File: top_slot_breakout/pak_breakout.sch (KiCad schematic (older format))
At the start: 19 parts, among them J1 Conn_02x08_Odd_Even, J2 Conn_01x06_Female, J3 Conn_01x04_Female, J4 Conn_01x02_Female, J5 Conn_01x03_Female, J6 Conn_01x12_Female, U1 74LS245, U2 74LS245, U3 Pico

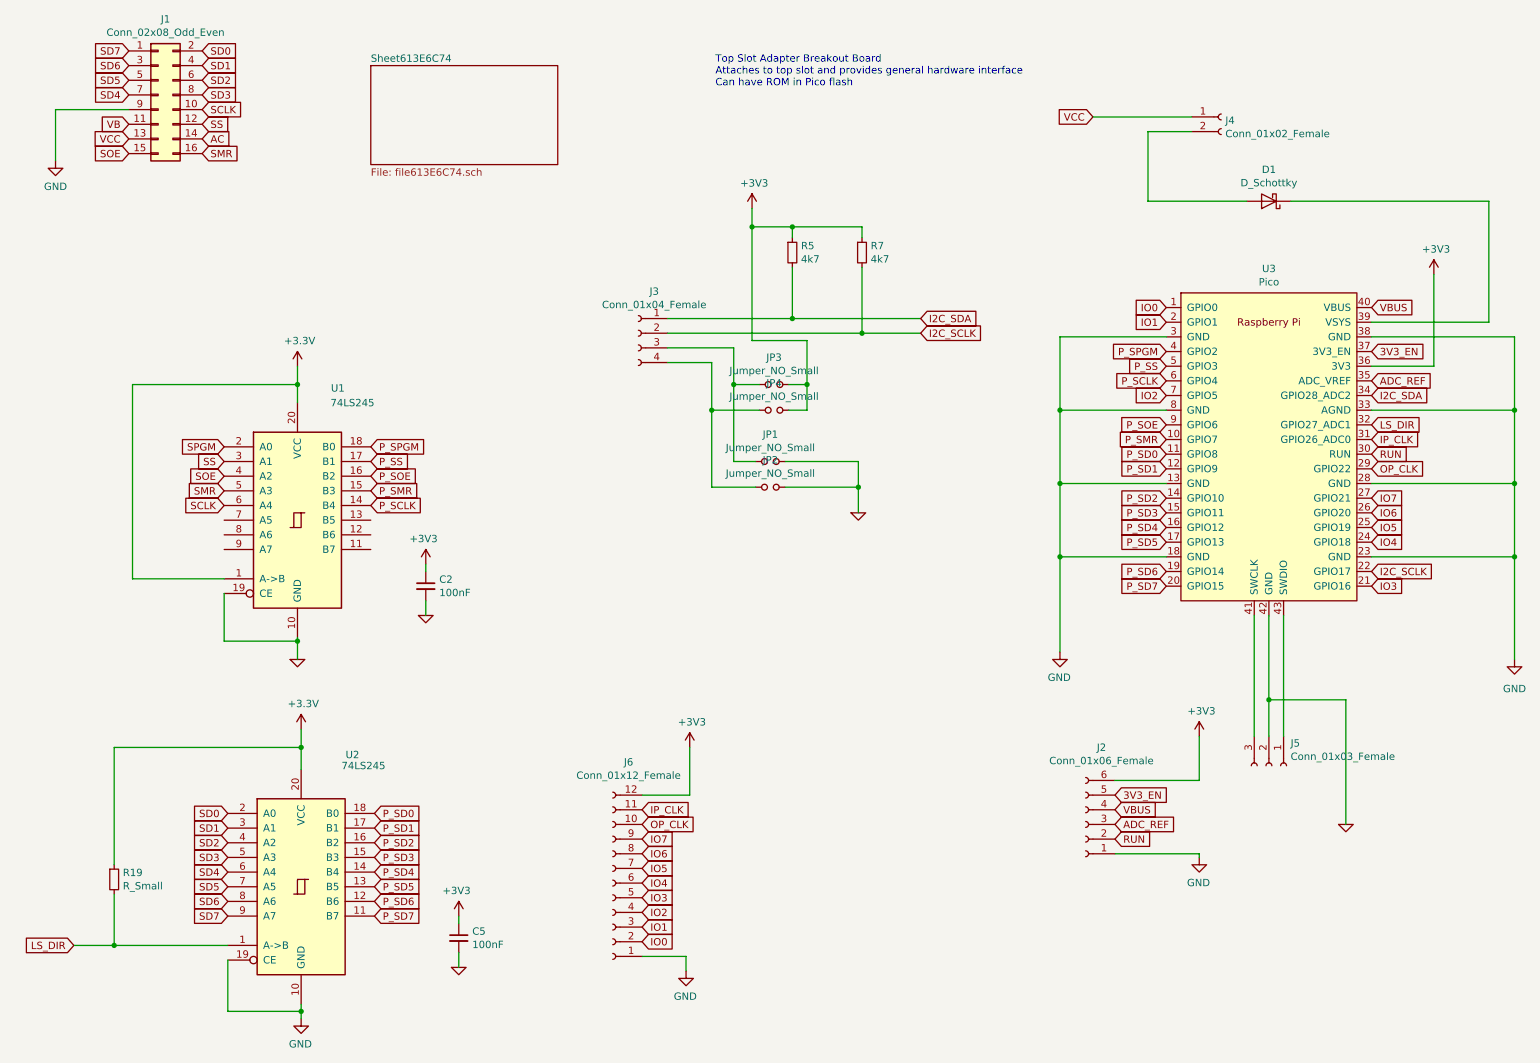
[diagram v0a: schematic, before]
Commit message: Added code based on (identical to) pak-gadget
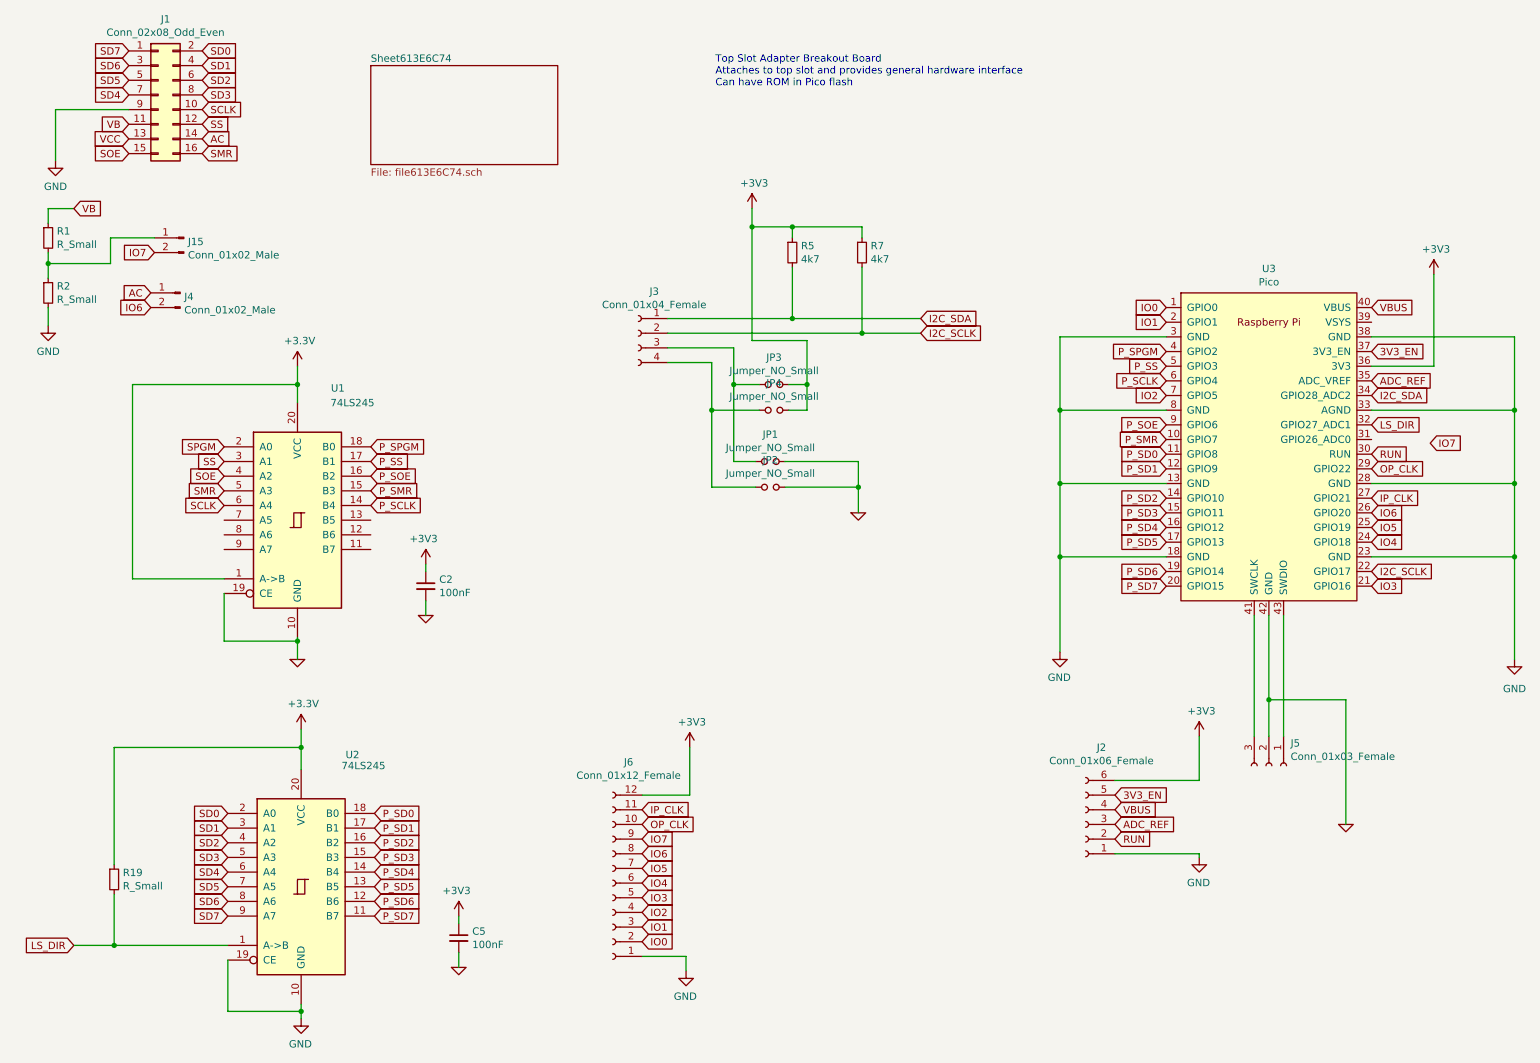
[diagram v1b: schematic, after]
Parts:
- removed D1: D_Schottky, Diode_SMD:D_SOD-123, symbol Device:D_Schottky
- removed J4: Conn_01x02_Female, Connector_PinHeader_2.54mm:PinHeader_1x02_P2.54mm_Vertical, symbol Connector:Conn_01x02_Female
- added J15, J4: Conn_01x02_Male, Connector_PinHeader_2.54mm:PinHeader_1x02_P2.54mm_Vertical, symbol Connector:Conn_01x02_Male
- added R1, R2: R_Small, Resistor_SMD:R_0805_2012Metric, symbol Device:R_Small
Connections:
- net AC: now also J4.1 (Pin_1)
- net GND: now also R2.2
- net IO6: now also J4.2 (Pin_2)
- net IO7: now also J15.2 (Pin_2); no longer U3.27 (GPIO21)
- net IP_CLK: now also U3.27 (GPIO21); no longer U3.31 (GPIO26_ADC0)
- net VB: now also R1.1
- new net: J15.1 (Pin_1), R1.2, R2.1
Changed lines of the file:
@@
 Wire Wire Line
 	3525 6975 3525 7075
-Wire Wire Line
-	9200 1850 10550 1850
-Wire Wire Line
-	10550 1850 10550 2675
-Wire Wire Line
-	10550 2675 9750 2675
-Wire Wire Line
-	8900 1850 8225 1850
-Wire Wire Line
-	8225 1850 8225 1375
-Wire Wire Line
-	8225 1375 8525 1375
-Text GLabel 7850 1275 0    50   Input ~ 0
-VCC
-Wire Wire Line
-	7850 1275 8525 1275
-$Comp
-L Device:D_Schottky D1
-U 1 1 60D0F436
-P 9050 1850
-F 0 "D1" H 9050 1634 50  0000 C CNN
-F 1 "D_Schottky" H 9050 1725 50  0000 C CNN
-F 2 "Diode_SMD:D_SOD-123" H 9050 1850 50  0001 C CNN
-F 3 "~" H 9050 1850 50  0001 C CNN
-	1    9050 1850
-	-1   0    0    1
-$EndComp
-$Comp
-L Connector:Conn_01x02_Female J4
-U 1 1 60D0E699
-P 8725 1275
-F 0 "J4" H 8753 1251 50  0000 L CNN
-F 1 "Conn_01x02_Female" H 8753 1160 50  0000 L CNN
-F 2 "Connector_PinHeader_2.54mm:PinHeader_1x02_P2.54mm_Vertical" H 8725 1275 50  0001 C CNN
-F 3 "~" H 8725 1275 50  0001 C CNN
-	1    8725 1275
-	1    0    0    -1
-$EndComp
 $Comp
 L pak_breakout-rescue:GND-Microtan_65_CPU-cache #PWR0129
@@
 Text GLabel 9750 3975 2    50   Input ~ 0
 IO6
-Text GLabel 9750 3875 2    50   Input ~ 0
+Text GLabel 10150 3500 2    50   Input ~ 0
 IO7
 Text GLabel 4775 6900 2    50   Input ~ 0
@@
 F1 "file613E6C74.sch" 50
 $EndSheet
-Text GLabel 9750 3475 2    50   Input ~ 0
+Text GLabel 9750 3875 2    50   Input ~ 0
 IP_CLK
 Text GLabel 9750 3675 2    50   Input ~ 0
@@
 Text GLabel 4775 6100 2    50   Input ~ 0
 OP_CLK
+$Comp
+L Connector:Conn_01x02_Male J15
+U 1 1 61462BE9
+P 1650 2100
+F 0 "J15" H 1622 2074 50  0000 R CNN
+F 1 "Conn_01x02_Male" H 1622 1983 50  0000 R CNN
+F 2 "Connector_PinHeader_2.54mm:PinHeader_1x02_P2.54mm_Vertical" H 1650 2100 50  0001 C CNN
+F 3 "~" H 1650 2100 50  0001 C CNN
+	1    1650 2100
+	-1   0    0    -1
+$EndComp
+Text GLabel 900  1900 2    50   Input ~ 0
+VB
+Text GLabel 1450 2200 0    50   Input ~ 0
+IO7
+$Comp
+L Connector:Conn_01x02_Male J4
+U 1 1 614671EB
+P 1625 2475
+F 0 "J4" H 1597 2449 50  0000 R CNN
+F 1 "Conn_01x02_Male" H 1597 2358 50  0000 R CNN
+F 2 "Connector_PinHeader_2.54mm:PinHeader_1x02_P2.54mm_Vertical" H 1625 2475 50  0001 C CNN
+F 3 "~" H 1625 2475 50  0001 C CNN
+	1    1625 2475
+	-1   0    0    -1
+$EndComp
+Text GLabel 1425 2475 0    50   Input ~ 0
+AC
+Text GLabel 1425 2575 0    50   Input ~ 0
+IO6
+$Comp
+L Device:R_Small R1
+U 1 1 614709EB
+P 725 2100
+F 0 "R1" H 784 2146 50  0000 L CNN
+F 1 "R_Small" H 784 2055 50  0000 L CNN
+F 2 "Resistor_SMD:R_0805_2012Metric" H 725 2100 50  0001 C CNN
+F 3 "~" H 725 2100 50  0001 C CNN
+	1    725  2100
+	1    0    0    -1
+$EndComp
+$Comp
+L Device:R_Small R2
+U 1 1 61471827
+P 725 2475
+F 0 "R2" H 784 2521 50  0000 L CNN
+F 1 "R_Small" H 784 2430 50  0000 L CNN
+F 2 "Resistor_SMD:R_0805_2012Metric" H 725 2475 50  0001 C CNN
+F 3 "~" H 725 2475 50  0001 C CNN
+	1    725  2475
+	1    0    0    -1
+$EndComp
+$Comp
+L power:GND #PWR0125
+U 1 1 61471EA7
+P 725 2700
+F 0 "#PWR0125" H 725 2450 50  0001 C CNN
+F 1 "GND" H 725 2525 50  0000 C CNN
+F 2 "" H 725 2700 50  0001 C CNN
+F 3 "" H 725 2700 50  0001 C CNN
+	1    725  2700
+	1    0    0    -1
+$EndComp
+Wire Wire Line
+	725  2700 725  2575
+Wire Wire Line
+	725  2200 725  2275
+Wire Wire Line
+	900  1900 725  1900
+Wire Wire Line
+	725  1900 725  2000
+Wire Wire Line
+	725  2275 1150 2275
+Wire Wire Line
+	1150 2275 1150 2100
+Wire Wire Line
+	1150 2100 1450 2100
+Connection ~ 725  2275
+Wire Wire Line
+	725  2275 725  2375
 $EndSCHEMATC
